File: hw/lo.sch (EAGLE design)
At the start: 47 parts, among them U1 ADF4360, X1 CLK, X2 DATA, X3 LE, X4 DIVOUT, X5 SMA-142-0701-881/886, X6 SMA-142-0701-881/886, X7 VIN

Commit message: use loop filter values from simulation
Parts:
- removed L3, L4: 220n, rcl:L-EUL4532C
- removed R6, R7: 56R, rcl:R-EU_R0603
- added R10, R9: 56R, rcl:R-EU_R0603
- C1: value 100p -> 1n5
- C2: value 1n -> 10n
- C3: value 47p -> (none)
- L1, L2: value 68n -> 30n
- R2: value 4k9 -> 12k
- R3: value 12k -> 0R
- U1: value ADF4360 -> ADF4360-9
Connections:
- net GND: no longer R6.2, R7.2
- net N$12: no longer R7.1
- net N$14: no longer R6.1
- net N$19: now also R9.2; no longer L3.2
- net N$20: now also R10.2; no longer L4.2
- net N$21: now also R10.1, R9.1; no longer L3.1, L4.1

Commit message: rev.1: finished lo board
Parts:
- removed C18: 10n, rcl:C-EUC0402
- removed C3: (no value), rcl:C-EUC0402
- removed FB3, FB6: BML15H, ferrite-bead:BML15H
- removed R3: 0R, rcl:R-EU_R0603
- L1, L2: device rcl:L-EUL4532C -> rcl:L-EUL2012C
- R8: device rcl:R-EU_R0603 -> rcl:R-EU_R0402
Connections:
- net N$11 renamed RUT
- removed net N$10: C3.1, R3.2, U1A.VTUNE
- removed net N$21: C18.1, FB6.1, R10.1, R9.1
- removed net N$27: C11.1, FB3.1, OSC1.E/D, OSC1.VCC
- removed net N$7: C1.1, C2.1, R3.1, U1D.CP
- new net LD: C1.1, C2.1, U1A.VTUNE, U1D.CP
- net +3V3: now also C11.1, OSC1.E/D, OSC1.VCC, R10.1, R9.1; no longer FB3.2, FB6.2
- net GND: no longer C18.2, C3.2
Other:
- note added: "Rev.: 1"
- note removed: "Rev.: 0"
- moved on the sheet: R10, R9

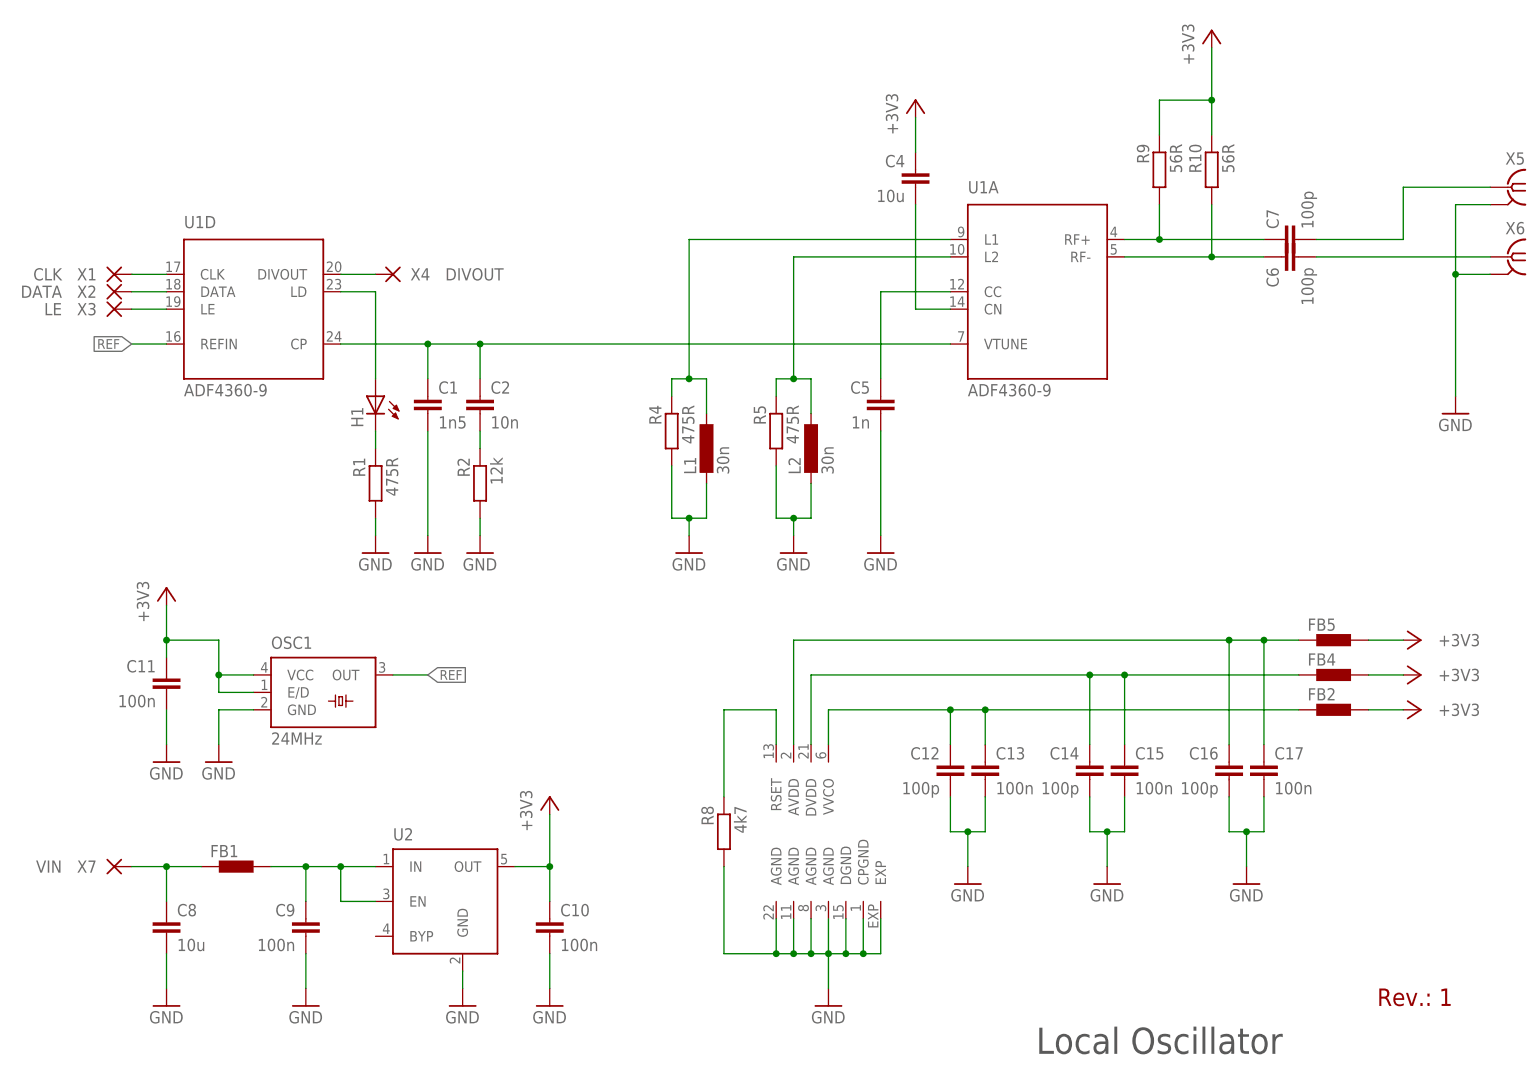
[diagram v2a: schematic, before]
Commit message: optimize layout for easier soldering
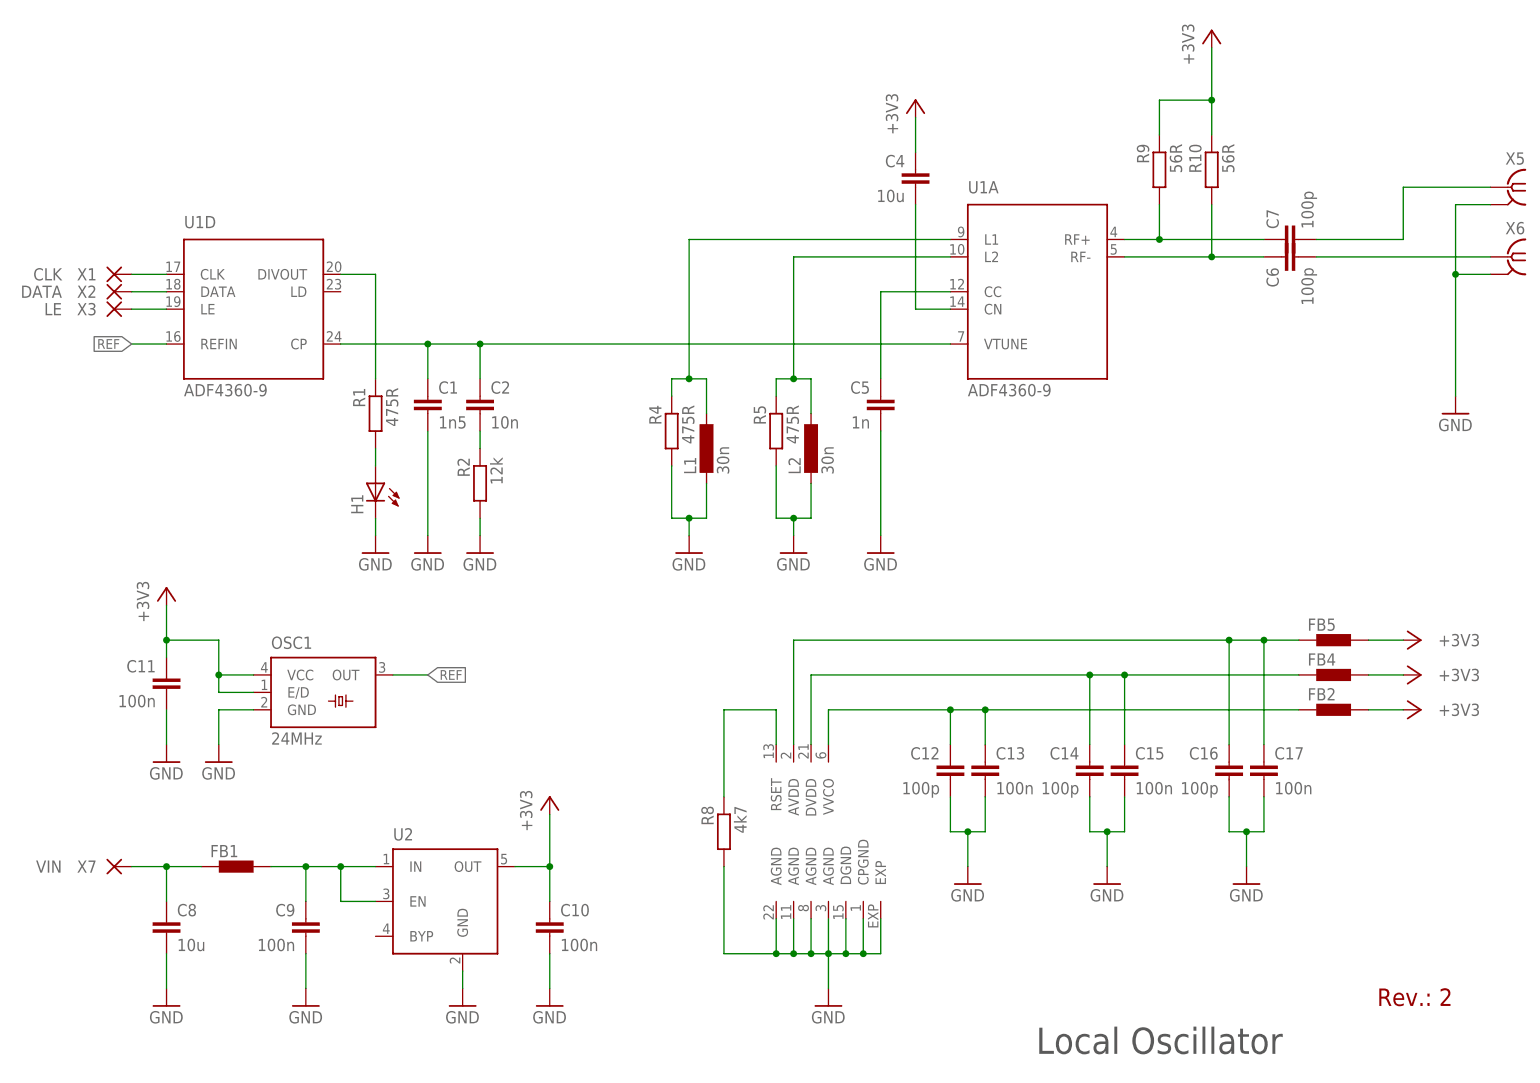
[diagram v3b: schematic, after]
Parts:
- removed X4: DIVOUT, wirepad:SMD2
- C11: device rcl:C-EUC0805 -> rcl:C-EUC0603
- C12, C13, C14, C15, C16, C17, C2, C5: device rcl:C-EUC0402 -> rcl:C-EUC0603
- R1: device rcl:R-EU_R0603 -> rcl:R-EU_R1206
- R8: device rcl:R-EU_R0402 -> rcl:R-EU_R0603
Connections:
- removed net N$8: U1D.DIVOUT, X4.P
- net GND: now also H1.C; no longer R1.2
- net N$5: now also R1.1, U1D.DIVOUT; no longer H1.A, U1D.LD
- net N$6: now also H1.A, R1.2; no longer H1.C, R1.1
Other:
- note added: "Rev.: 2"
- note removed: "Rev.: 1"
- moved on the sheet: H1, R1
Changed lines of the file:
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@@
 <setting verticaltext="up"/>
 </settings>
-<grid distance="0.1" unitdist="inch" unit="inch" style="lines" multiple="1" display="no" altdistance="0.01" altunitdist="inch" altunit="inch"/>
+<grid distance="0.1" unitdist="inch" unit="inch" style="dots" multiple="1" display="yes" altdistance="0.01" altunitdist="inch" altunit="inch"/>
 <layers>
 <layer number="1" name="Top" color="4" fill="1" visible="no" active="no"/>
@@
 <part name="GND2" library="supply1" deviceset="GND" device=""/>
 <part name="GND3" library="supply1" deviceset="GND" device=""/>
-<part name="R1" library="rcl" deviceset="R-EU_" device="R0603" value="475R"/>
-<part name="X4" library="wirepad" deviceset="SMD2" device="" value="DIVOUT"/>
+<part name="R1" library="rcl" deviceset="R-EU_" device="R1206" value="475R"/>
 <part name="C1" library="rcl" deviceset="C-EU" device="C0402" value="1n5"/>
 <part name="GND4" library="supply1" deviceset="GND" device=""/>
-<part name="C2" library="rcl" deviceset="C-EU" device="C0402" value="10n"/>
+<part name="C2" library="rcl" deviceset="C-EU" device="C0603" value="10n"/>
 <part name="R2" library="rcl" deviceset="R-EU_" device="R0603" value="12k"/>
 <part name="GND5" library="supply1" deviceset="GND" device=""/>
@@
 <part name="L2" library="rcl" deviceset="L-EU" device="L2012C" value="30n"/>
 <part name="GND8" library="supply1" deviceset="GND" device=""/>
-<part name="C5" library="rcl" deviceset="C-EU" device="C0402" value="1n"/>
+<part name="C5" library="rcl" deviceset="C-EU" device="C0603" value="1n"/>
 <part name="GND9" library="supply1" deviceset="GND" device=""/>
 <part name="C6" library="rcl" deviceset="C-EU" device="C0402" value="100p"/>
@@
 <part name="GND16" library="supply1" deviceset="GND" device=""/>
 <part name="GND17" library="supply1" deviceset="GND" device=""/>
-<part name="C11" library="rcl" deviceset="C-EU" device="C0805" value="100n"/>
+<part name="C11" library="rcl" deviceset="C-EU" device="C0603" value="100n"/>
 <part name="+3V2" library="supply1" deviceset="+3V3" device=""/>
-<part name="R8" library="rcl" deviceset="R-EU_" device="R0402" value="4k7"/>
-<part name="C12" library="rcl" deviceset="C-EU" device="C0402" value="100p"/>
-<part name="C13" library="rcl" deviceset="C-EU" device="C0402" value="100n"/>
-<part name="C14" library="rcl" deviceset="C-EU" device="C0402" value="100p"/>
-<part name="C15" library="rcl" deviceset="C-EU" device="C0402" value="100n"/>
-<part name="C16" library="rcl" deviceset="C-EU" device="C0402" value="100p"/>
-<part name="C17" library="rcl" deviceset="C-EU" device="C0402" value="100n"/>
+<part name="R8" library="rcl" deviceset="R-EU_" device="R0603" value="4k7"/>
+<part name="C12" library="rcl" deviceset="C-EU" device="C0603" value="100p"/>
+<part name="C13" library="rcl" deviceset="C-EU" device="C0603" value="100n"/>
+<part name="C14" library="rcl" deviceset="C-EU" device="C0603" value="100p"/>
+<part name="C15" library="rcl" deviceset="C-EU" device="C0603" value="100n"/>
+<part name="C16" library="rcl" deviceset="C-EU" device="C0603" value="100p"/>
+<part name="C17" library="rcl" deviceset="C-EU" device="C0603" value="100n"/>
 <part name="FB4" library="ferrite-bead" deviceset="BML15H" device="" value=""/>
 <part name="FB5" library="ferrite-bead" deviceset="BML15H" device="" value=""/>
@@
 <plain>
 <text x="185.42" y="15.24" size="3.81" layer="97" align="center">Local Oscillator</text>
-<text x="217.17" y="20.32" size="2.54" layer="94" font="vector">Rev.: 1</text>
+<text x="217.17" y="20.32" size="2.54" layer="94" font="vector">Rev.: 2</text>
 </plain>
 <instances>
@@
 </instance>
 <instance part="OSC1" gate="G$1" x="63.5" y="66.04"/>
-<instance part="H1" gate="G$1" x="71.12" y="109.22" rot="MR0"/>
+<instance part="H1" gate="G$1" x="71.12" y="96.52" rot="MR0"/>
 <instance part="+3V1" gate="G$1" x="96.52" y="50.8"/>
 <instance part="GND1" gate="1" x="83.82" y="20.32"/>
 <instance part="GND2" gate="1" x="137.16" y="20.32"/>
 <instance part="GND3" gate="1" x="71.12" y="86.36"/>
-<instance part="R1" gate="G$1" x="71.12" y="96.52" rot="MR270"/>
-<instance part="X4" gate="1" x="73.66" y="127" smashed="yes" rot="R180">
-<attribute name="NAME" x="76.2" y="127" size="1.778" layer="95" rot="R180" align="center-right"/>
-<attribute name="VALUE" x="81.28" y="127" size="1.778" layer="96" rot="R180" align="center-right"/>
-</instance>
+<instance part="R1" gate="G$1" x="71.12" y="106.68" rot="MR270"/>
 <instance part="C1" gate="G$1" x="78.74" y="109.22"/>
 <instance part="GND4" gate="1" x="78.74" y="86.36"/>
@@
 <net name="N$5" class="0">
 <segment>
-<pinref part="U1" gate="D" pin="LD"/>
-<pinref part="H1" gate="G$1" pin="A"/>
-<wire x1="66.04" y1="124.46" x2="71.12" y2="124.46" width="0.1524" layer="91"/>
-<wire x1="71.12" y1="124.46" x2="71.12" y2="111.76" width="0.1524" layer="91"/>
+<pinref part="U1" gate="D" pin="DIVOUT"/>
+<wire x1="66.04" y1="127" x2="71.12" y2="127" width="0.1524" layer="91"/>
+<pinref part="R1" gate="G$1" pin="1"/>
+<wire x1="71.12" y1="127" x2="71.12" y2="111.76" width="0.1524" layer="91"/>
 </segment>
 </net>
 <net name="GND" class="0">
-<segment>
-<pinref part="GND3" gate="1" pin="GND"/>
-<pinref part="R1" gate="G$1" pin="2"/>
-<wire x1="71.12" y1="88.9" x2="71.12" y2="91.44" width="0.1524" layer="91"/>
-</segment>
 <segment>
 <pinref part="C1" gate="G$1" pin="2"/>
@@
 <junction x="198.12" y="45.72"/>
 </segment>
-</net>
-<net name="N$6" class="0">
-<segment>
-<pinref part="R1" gate="G$1" pin="1"/>
+<segment>
 <pinref part="H1" gate="G$1" pin="C"/>
-<wire x1="71.12" y1="104.14" x2="71.12" y2="101.6" width="0.1524" layer="91"/>
-</segment>
-</net>
-<net name="N$8" class="0">
-<segment>
-<pinref part="U1" gate="D" pin="DIVOUT"/>
-<pinref part="X4" gate="1" pin="P"/>
-<wire x1="66.04" y1="127" x2="71.12" y2="127" width="0.1524" layer="91"/>
+<pinref part="GND3" gate="1" pin="GND"/>
+<wire x1="71.12" y1="91.44" x2="71.12" y2="88.9" width="0.1524" layer="91"/>
 </segment>
 </net>
@@
 </segment>
 </net>
+<net name="N$6" class="0">
+<segment>
+<pinref part="R1" gate="G$1" pin="2"/>
+<pinref part="H1" gate="G$1" pin="A"/>
+<wire x1="71.12" y1="101.6" x2="71.12" y2="99.06" width="0.1524" layer="91"/>
+</segment>
+</net>
